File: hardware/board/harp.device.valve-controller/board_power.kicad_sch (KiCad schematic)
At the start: 22 parts, among them J8 Screw_Terminal_01x02, Q2 GSFD4005, U7 rt6150b-33gqw, U9 MCP16312x-xMNY

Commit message: route pcb
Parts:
- F1: Link https://www.digikey.com/en/products/detail/littelfuse-inc/2920L600-24SLER/12807028 -> https://www.digikey.com/en/products/detail/littelfuse-inc/2920L700-24SLER/12807015; Manufacturer Number 2920L600/24SLER -> 2920L700/24SLER
- Q2: Link (none) -> https://www.digikey.com/en/products/detail/good-ark-semicon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; Manufacturer Number (none) -> GSFD4005
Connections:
- net +3V3 renamed +3.3V
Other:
- note added: "Resettable Fuse: 7A Holding 14A Trip"
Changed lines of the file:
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@@
+		)
+	)
+	(text "Resettable Fuse:\n7A Holding\n14A Trip"
+		(exclude_from_sim no)
+		(at 101.6 44.45 0)
+		(effects
+			(font
+				(size 1.27 1.27)
+			)
+			(justify left bottom)
 		)
 	)
@@
 		(on_board yes)
 		(dnp no)
-		(fields_autoplaced yes)
 		(property "Reference" "#PWR061"
 			(at 110.49 54.61 0)
@@
 		)
 		(property "Value" "VPP"
-			(at 110.49 45.72 0)
+			(at 110.49 46.99 0)
 			(effects
 				(font
@@
 		(on_board yes)
 		(dnp no)
-		(fields_autoplaced yes)
 		(property "Reference" "F1"
-			(at 105.41 48.26 90)
+			(at 105.41 52.07 90)
 			(effects
 				(font
@@
 					(size 1.27 1.27)
 				)
+				(hide yes)
 			)
 		)
@@
 			)
 		)
-		(property "Description" "Resettable fuse, 24V max, 6A holding, 12A trip"
+		(property "Description" "Resettable fuse, 24V max, 7A holding, 14A trip"
 			(at 105.41 54.61 0)
 			(effects
@@
 			)
 		)
-		(property "Manufacturer Number" "2920L600/24SLER"
+		(property "Manufacturer Number" "2920L700/24SLER"
 			(at 105.41 54.61 90)
 			(effects
@@
 			)
 		)
-		(property "Link" "https://www.digikey.com/en/products/detail/littelfuse-inc/2920L600-24SLER/12807028"
+		(property "Link" "https://www.digikey.com/en/products/detail/littelfuse-inc/2920L700-24SLER/12807015"
 			(at 105.41 54.61 90)
 			(effects
@@
 				(path "/e63e39d7-6ac0-4ffd-8aa3-1841a4541b55/b51b21ef-b374-4f9f-a058-7db9b64fdf4a"
 					(reference "L5")
+					(unit 1)
+				)
+			)
+		)
+	)
+	(symbol
+		(lib_id "power:+3.3V")
+		(at 167.64 116.84 0)
+		(unit 1)
+		(exclude_from_sim no)
+		(in_bom yes)
+		(on_board yes)
+		(dnp no)
+		(fields_autoplaced yes)
+		(property "Reference" "#PWR048"
+			(at 167.64 120.65 0)
+			(effects
+				(font
+					(size 1.27 1.27)
+				)
+				(hide yes)
+			)
+		)
+		(property "Value" "+3.3V"
+			(at 167.64 111.76 0)
+			(effects
+				(font
+					(size 1.27 1.27)
+				)
+			)
+		)
+		(property "Footprint" ""
+			(at 167.64 116.84 0)
+			(effects
+				(font
+					(size 1.27 1.27)
+				)
+				(hide yes)
+			)
+		)
+		(property "Datasheet" ""
+			(at 167.64 116.84 0)
+			(effects
+				(font
+					(size 1.27 1.27)
+				)
+				(hide yes)
+			)
+		)
+		(property "Description" "Power symbol creates a global label with name \"+3.3V\""
+			(at 167.64 116.84 0)
+			(effects
+				(font
+					(size 1.27 1.27)
+				)
+				(hide yes)
+			)
+		)
+		(pin "1"
+		)
+		(instances
+			(project ""
+				(path "/e63e39d7-6ac0-4ffd-8aa3-1841a4541b55/b51b21ef-b374-4f9f-a058-7db9b64fdf4a"
+					(reference "#PWR048")
 					(unit 1)
 				)
@@
 	)
 	(symbol
-		(lib_id "power:+3V3")
-		(at 167.64 116.84 0)
-		(unit 1)
-		(exclude_from_sim no)
-		(in_bom yes)
-		(on_board yes)
-		(dnp no)
-		(property "Reference" "#PWR048"
-			(at 167.64 120.65 0)
-			(effects
-				(font
-					(size 1.27 1.27)
-				)
-				(hide yes)
-			)
-		)
-		(property "Value" "+3V3"
-			(at 167.64 113.03 0)
-			(effects
-				(font
-					(size 1.27 1.27)
-				)
-			)
-		)
-		(property "Footprint" ""
-			(at 167.64 116.84 0)
-			(effects
-				(font
-					(size 1.27 1.27)
-				)
-				(hide yes)
-			)
-		)
-		(property "Datasheet" ""
-			(at 167.64 116.84 0)
-			(effects
-				(font
-					(size 1.27 1.27)
-				)
-				(hide yes)
-			)
-		)
-		(property "Description" ""
-			(at 167.64 116.84 0)
-			(effects
-				(font
-					(size 1.27 1.27)
-				)
-				(hide yes)
-			)
-		)
-		(pin "1"
-		)
-		(instances
-			(project "valve-controller"
-				(path "/e63e39d7-6ac0-4ffd-8aa3-1841a4541b55/b51b21ef-b374-4f9f-a058-7db9b64fdf4a"
-					(reference "#PWR048")
-					(unit 1)
-				)
-			)
-		)
-	)
-	(symbol
 		(lib_id "Transistor_FET:SUD45P03-09")
 		(at 91.44 57.15 90)
@@
 			)
 		)
-		(property "Description" ""
+		(property "Description" "P-Channel Mosfet, -88A"
 			(at 91.44 57.15 0)
 			(effects
 				(font
+					(size 1.27 1.27)
+				)
+				(hide yes)
+			)
+		)
+		(property "Link" "https://www.digikey.com/en/products/detail/good-ark-semiconductor/GSFD4005/22168140"
+			(at 91.44 57.15 90)
+			(effects
+				(font
+					(size 1.27 1.27)
+				)
+				(hide yes)
+			)
+		)
+		(property "Manufacturer Number" "GSFD4005"
+			(at 91.44 57.15 90)
+			(effects
+				(font

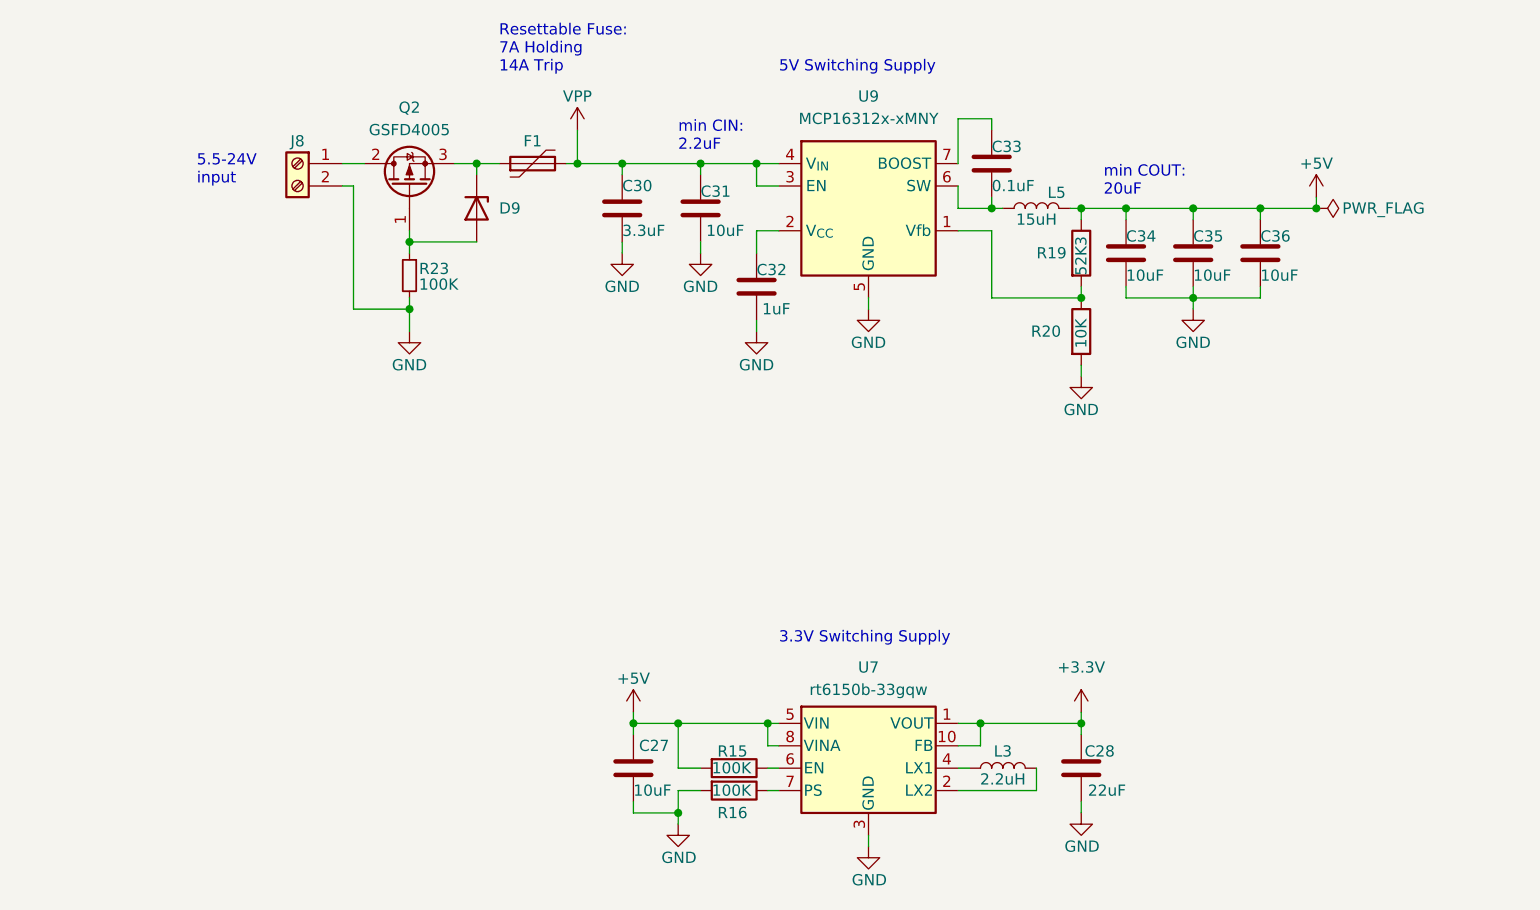
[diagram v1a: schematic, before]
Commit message: update pcb power supply
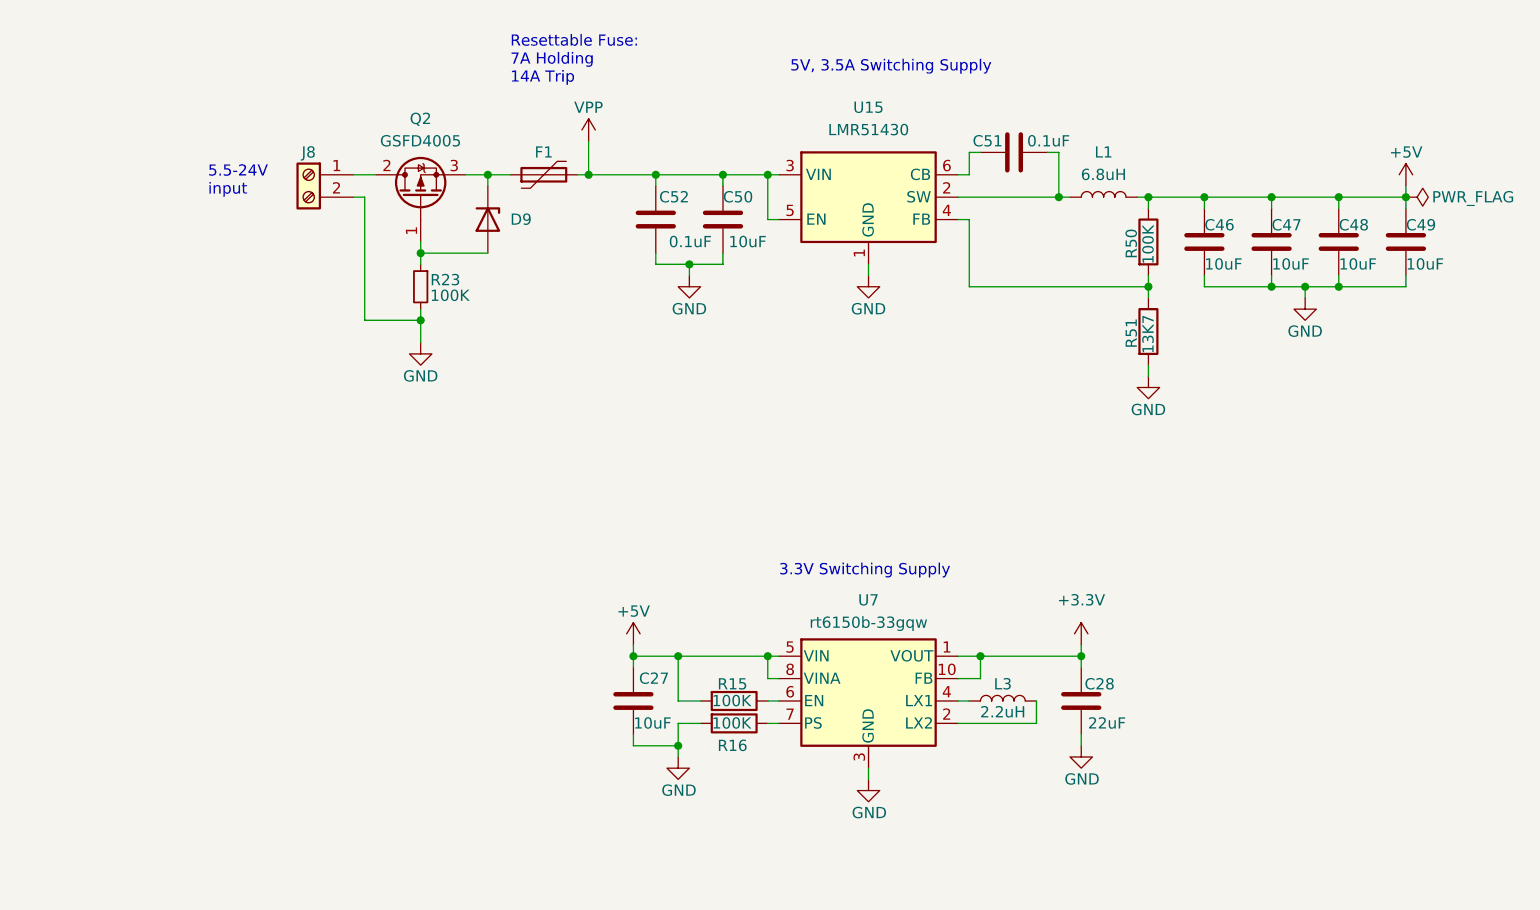
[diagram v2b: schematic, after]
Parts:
- removed C30: 3.3uF, Capacitor_SMD:C_0805_2012Metric, symbol Device:C
- removed C31, C34, C35, C36: 10uF, Capacitor_SMD:C_0805_2012Metric, symbol Device:C
- removed C32: 1uF, Capacitor_SMD:C_0805_2012Metric, symbol Device:C
- removed C33: 0.1uF, Capacitor_SMD:C_0603_1608Metric, symbol Device:C
- removed L5: 15uH, kicad_component_library:L_Wuerth_5.5x5.3mm, symbol Device:L
- removed R19: 52K3, Resistor_SMD:R_0603_1608Metric, symbol Device:R
- removed R20: 10K, Resistor_SMD:R_0603_1608Metric, symbol Device:R
- removed U9: MCP16312x-xMNY, Package_DFN_QFN:DFN-8-1EP_3x2mm_P0.5mm_EP1.75x1.45mm, symbol Regulator_Switching:MCP16312x-xMNY
- added C46, C47, C48, C49, C50: 10uF, Capacitor_SMD:C_0805_2012Metric, symbol Device:C
- added C51, C52: 0.1uF, Capacitor_SMD:C_0603_1608Metric, symbol Device:C
- added L1: 6.8uH, Inductor_SMD:L_Bourns_SRR1260, symbol Device:L
- added R50: 100K, Resistor_SMD:R_0402_1005Metric, symbol Device:R
- added R51: 13K7, Resistor_SMD:R_0402_1005Metric, symbol Device:R
- added U15: LMR51430, Package_TO_SOT_SMD:SOT-23-6, symbol Regulator_Switching:LMR51430
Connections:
- net +5V: now also C46.1, C47.1, C48.1, C49.1, L1.2, R50.1
- net GND: now also C46.2, C47.2, C48.2, C49.2, C50.2, C52.1, R51.2, U15.1 (GND)
- net VPP: now also C50.1, C52.2, U15.3 (VIN), U15.5 (EN)
- new net: C51.1, U15.6 (CB)
- new net: C51.2, L1.1, U15.2 (SW)
- new net: R50.2, R51.1, U15.4 (FB)
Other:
- note added: "5V, 3.5A Switching Supply"
- note removed: "5V Switching Supply"
- note removed: "min CIN: 2.2uF"
- note removed: "min COUT: 20uF"
- moved on the sheet: C27, C28, D9, F1, J8, L3, Q2, R15, R16, R23, U7

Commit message: update bom
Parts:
- J8: Link (none) -> https://www.digikey.com/en/products/detail/phoenix-contact/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; Manufacturer (none) -> Phoenix Contact; Manufacturer Number (none) -> 1757242; Notes (none) -> mates with Phoenix Contact 1758364
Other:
- note added: "5V, 3A Switching Supply"
- note added: "Mates w/ Phoenix Contact 1758364"
- note removed: "5V, 3.5A Switching Supply"
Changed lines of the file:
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@@
 		)
 	)
-	(text "5V, 3.5A Switching Supply"
+	(text "Mates w/\nPhoenix Contact\n1758364"
+		(exclude_from_sim no)
+		(at 46.99 60.96 0)
+		(effects
+			(font
+				(size 1.27 1.27)
+			)
+			(justify left bottom)
+		)
+	)
+	(text "5V, 3A Switching Supply"
 		(exclude_from_sim no)
 		(at 134.62 44.45 0)
@@
 			)
 		)
-		(property "Datasheet" "~"
+		(property "Datasheet" "https://www.phoenixcontact.com/en-us/products/pcb-header-mstba-25-2-g-508-1757242?type=pdf"
 			(at 80.01 55.88 0)
 			(effects
@@
 			(at 80.01 55.88 0)
 			(effects
+				(font
+					(size 1.27 1.27)
+				)
+				(hide yes)
+			)
+		)
+		(property "Manufacturer" "Phoenix Contact"
+			(at 80.01 55.88 0)
+			(effects
+				(font
+					(size 1.27 1.27)
+				)
+				(hide yes)
+			)
+		)
+		(property "Manufacturer Number" "1757242"
+			(at 80.01 55.88 0)
+			(effects
+				(font
+					(size 1.27 1.27)
+				)
+				(hide yes)
+			)
+		)
+		(property "Link" "https://www.digikey.com/en/products/detail/phoenix-contact/1757242/260474"
+			(at 80.01 55.88 0)
+			(effects
+				(font
+					(size 1.27 1.27)
+				)
+				(hide yes)
+			)
+		)
+		(property "Notes" "mates with Phoenix Contact 1758364"
+			(at 80.01 55.88 0)
+			(effects

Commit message: prep hw initial release
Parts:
- removed C49: 10uF, Capacitor_SMD:C_0805_2012Metric, symbol Device:C
- removed R23: 100K, Resistor_SMD:R_0603_1608Metric, symbol Device:R_Small
- added R23: 100K, Resistor_SMD:R_0402_1005Metric, symbol Device:R
- C27: Link https://www.digikey.com/en/products/detail/murata-electroni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 -> https://www.digikey.com/en/products/detail/cal-chip-electro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; Manufacturer Murata Electronics -> Cal-Chip Electronics, Inc.; Manufacturer Number GRM21BZ71E106KE15L -> GMC21X7R106K25NT; Rated Voltage 25V -> (none); Temperature Coefficient X7R -> (none)
- C46, C47, C48: value 10uF -> 22uF; Link https://www.digikey.com/en/products/detail/cal-chip-electro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 -> https://www.digikey.com/en/products/detail/samsung-electro-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; Manufacturer Cal-Chip Electronics, Inc. -> Samsung Electro-Mechanics; Manufacturer Number GMC21X7R106K25NT -> CL21A226KPCLRNC; Rated Voltage (none) -> 10V; Temperature Coefficient (none) -> X5R
- C51, C52: value 0.1uF -> 100nF; footprint Capacitor_SMD:C_0603_1608Metric -> Capacitor_SMD:C_0402_1005Metric; Link https://www.digikey.com/en/products/detail/tdk-corporation/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 -> https://www.digikey.com/en/products/detail/murata-electroni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; Manufacturer TDK Corporation -> Murata Electronics; Manufacturer Number CGA3E2X7R1H104K080AA -> GRM155R71H104KE14D; PCBWay Link (none) -> https://www.pcbway.com/components/detail/0402B104K160CT/307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; Rated Voltage (none) -> 50V; Temperature Coefficient (none) -> X7R; Tolerance (none) -> 10%
- D9: Link (none) -> https://www.digikey.com/en/products/detail/nexperia-usa-inc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; Manufacturer (none) -> Nexperia USA Inc.; Manufacturer Number (none) -> BZV55-B15,115
- F1: Manufacturer (none) -> Littelfuse Inc.
- Q2: Manufacturer (none) -> Good-Ark Semiconductor
- U15: Link (none) -> https://www.digikey.com/en/products/detail/texas-instrument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; Manufacturer (none) -> Texas Instruments; Manufacturer Number (none) -> LMR51430YDDCR; Notes (none) -> PFM version, 1.1MHz switching frequency
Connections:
- net +5V: now also C46.2, C47.2, C48.2; no longer C46.1, C47.1, C48.1
- net GND: now also C46.1, C47.1, C48.1, R23.2; no longer C46.2, C47.2, C48.2
- net at C51.1: now also L1.1, U15.2 (SW); no longer U15.6 (CB)
- net at D9.2 (A), Q2.1 (G): now also R23.1
- new net: C51.2, U15.6 (CB)
